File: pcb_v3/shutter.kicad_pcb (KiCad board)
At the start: 2 copper layers, 39 parts, among them IC1 ATMEGA328P-A, K1 FINDER-36.11, K2 FINDER-36.11, K3 HF49FD, P1 5V_IN, P2 GND5, P3 TX/RX, P4 CONN_01X05, P5 ISP, P6 ANT, P7 NETZ_N, P8 NETZ_L, P9 MOTOR, Q1 BC817, Q2 BC817, Q3 BC817, Y1 8MHZ

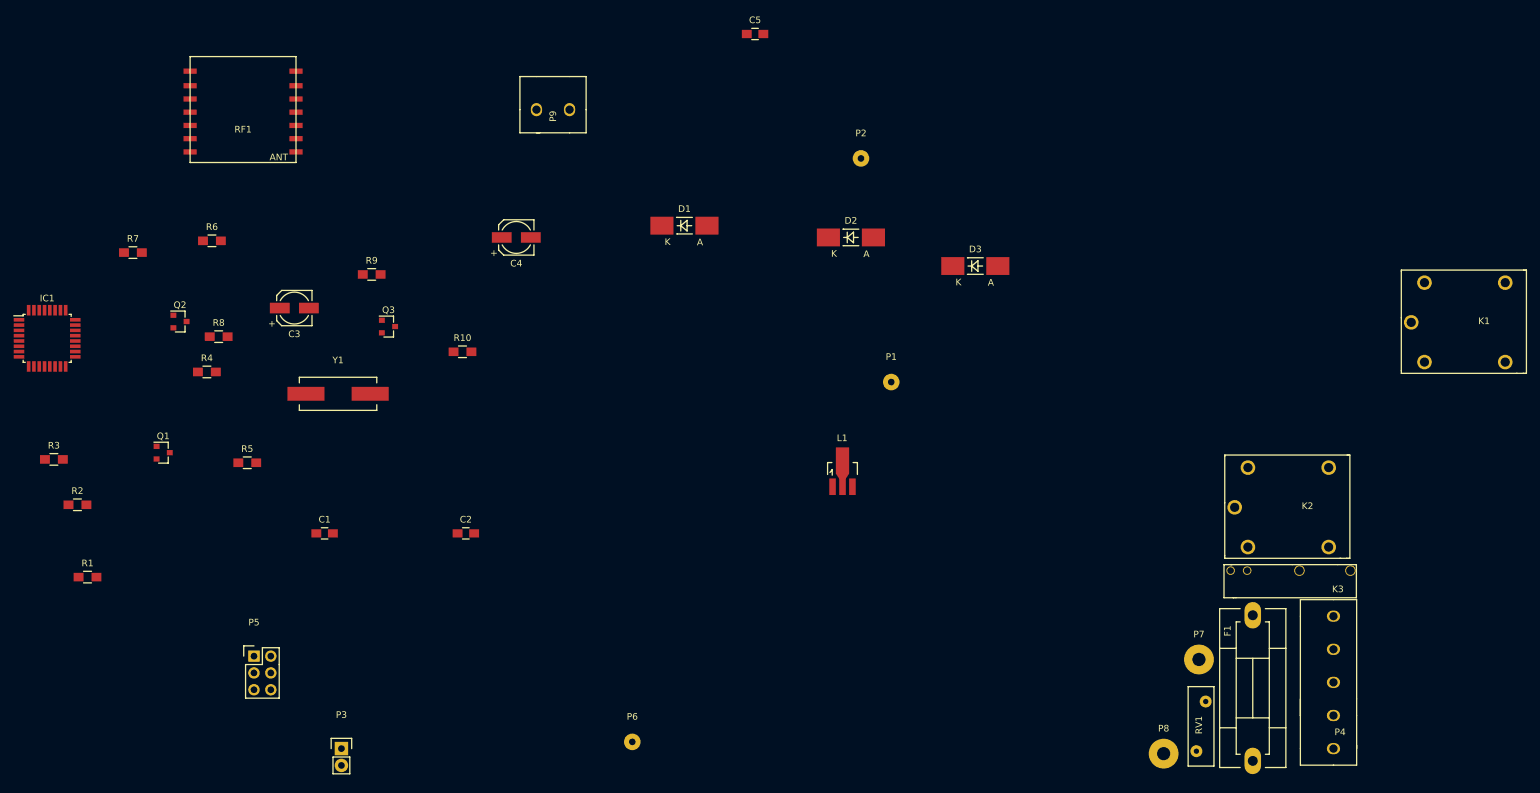
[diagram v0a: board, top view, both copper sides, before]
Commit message: added new Pcb
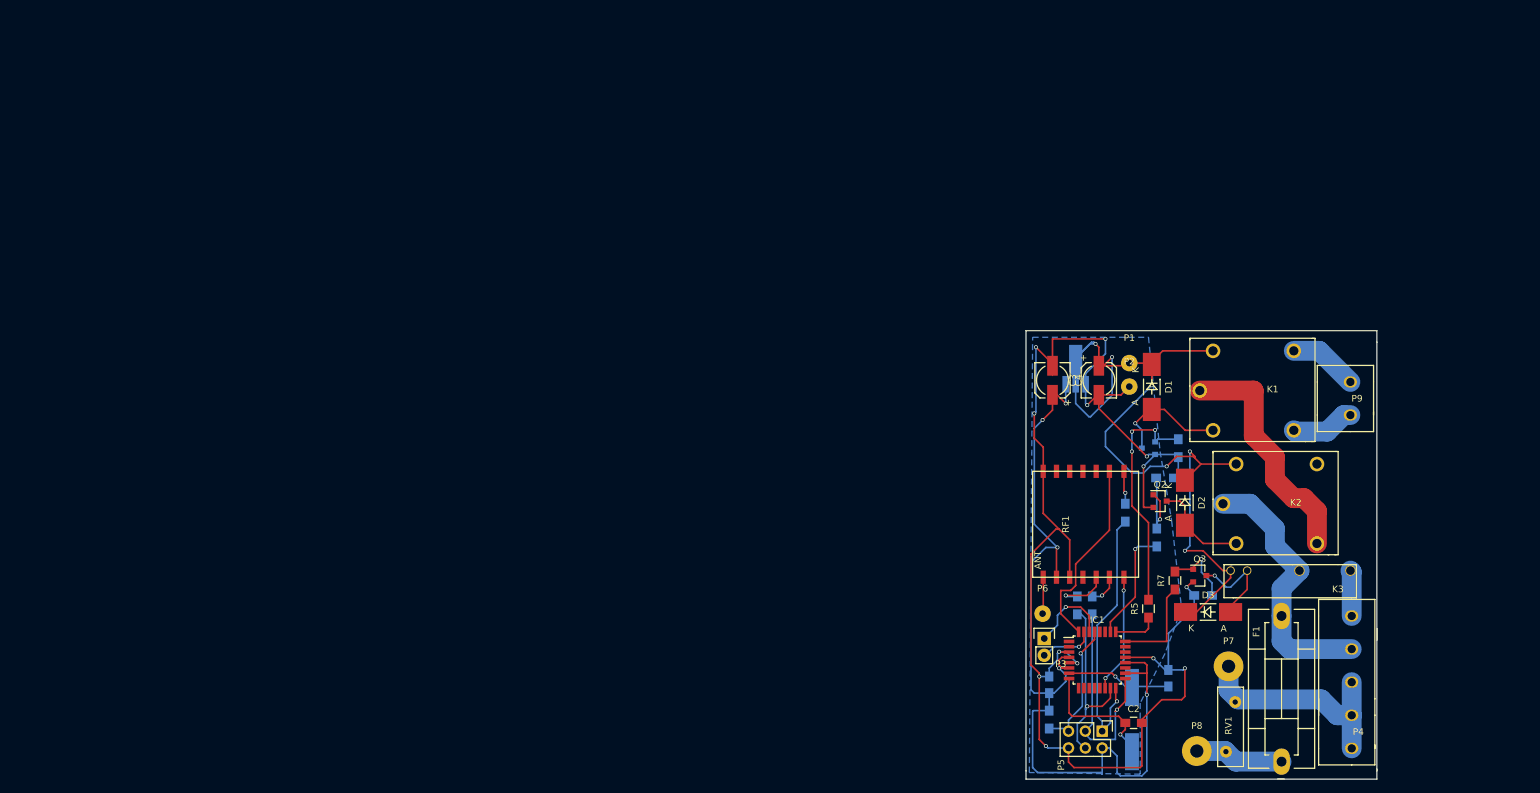
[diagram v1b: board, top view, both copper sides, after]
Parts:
- C1, C5, L1, Q1, R1, R10, R2, R3, R4, R6, R8, R9, Y1: moved to B.Cu
- moved IC1 165.9 mm to (214.8, 122.2)
- moved R7 165.0 mm to (226.5, 110.2), turned to 90 degrees
- moved R3 158.4 mm to (214.0, 114.0), turned to 270 degrees
- moved R2 158.3 mm to (219.0, 100.0), turned to 270 degrees
- moved Q2 150.5 mm to (224.2, 98.2)
- moved R6 149.6 mm to (223.8, 103.8), turned to 90 degrees
- moved Q1 148.8 mm to (222.5, 90.2), turned to 180 degrees
- moved RF1 147.2 mm to (214.0, 93.8), turned to 270 degrees
- moved R1 146.9 mm to (207.5, 131.2), turned to 270 degrees
- moved R8 144.5 mm to (225.0, 94.8), turned to 180 degrees
- moved R5 137.9 mm to (222.5, 114.5), turned to 90 degrees
- moved R4 136.1 mm to (211.8, 114.0), turned to 270 degrees
- moved P9 131.3 mm to (253.0, 85.2), turned to 90 degrees
- moved Y1 129.6 mm to (220.0, 131.2), turned to 270 degrees
- moved C1 129.3 mm to (225.5, 125.0), turned to 90 degrees
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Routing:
- net GND: track 0.00 -> 214.3 mm, vias 0 -> 13
- net 3.3V: track 0.00 -> 135.5 mm, vias 0 -> 5
- net 5V: track 0.00 -> 127.9 mm, vias 0 -> 6
- net MISO: track 0.00 -> 41.2 mm, vias 0 -> 1
- net L: track 0.00 -> 40.2 mm
- net Net-(K1-Pad11): track 0.00 -> 36.1 mm
- net Net-(Q1-Pad1): track 0.00 -> 35.5 mm, vias 0 -> 3
- net SCK: track 0.00 -> 33.9 mm, vias 0 -> 1
- net Net-(P4-Pad1): track 0.00 -> 33.8 mm
- net Net-(IC1-Pad32): track 0.00 -> 29.3 mm
- net MOSI: track 0.00 -> 28.4 mm, vias 0 -> 1
- net RST: track 0.00 -> 19.9 mm, vias 0 -> 1
- net XTAL2: track 0.00 -> 19.7 mm, vias 0 -> 1
- net Net-(D1-Pad2): track 0.00 -> 18.1 mm, vias 0 -> 1
- net NSS: track 0.00 -> 17.9 mm, vias 0 -> 2
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- added copper zone on B.Cu, net GND
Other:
- board outline added: 53 x 67.8 mm
- net class 220 added: clearance 1.5, trace_width 3, via_dia 0.6, via_drill 0.4
- net class std added: clearance 0.2, trace_width 0.25, via_dia 0.6, via_drill 0.4

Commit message: updated pcb
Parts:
- moved P9 1.75 mm to (253.0, 83.5)
- moved P4 0.45 mm to (253.0, 136.0)
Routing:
- net Net-(K1-Pad14): track 10.5 -> 9.77 mm
- net Net-(K1-Pad12): track 9.67 -> 10.2 mm
- net L: track 40.2 -> 39.7 mm
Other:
- net class Default: clearance 0.2 -> 1.3; trace_width 0.25 -> 3
- rule trace_clearance: 0.2 -> 1.3

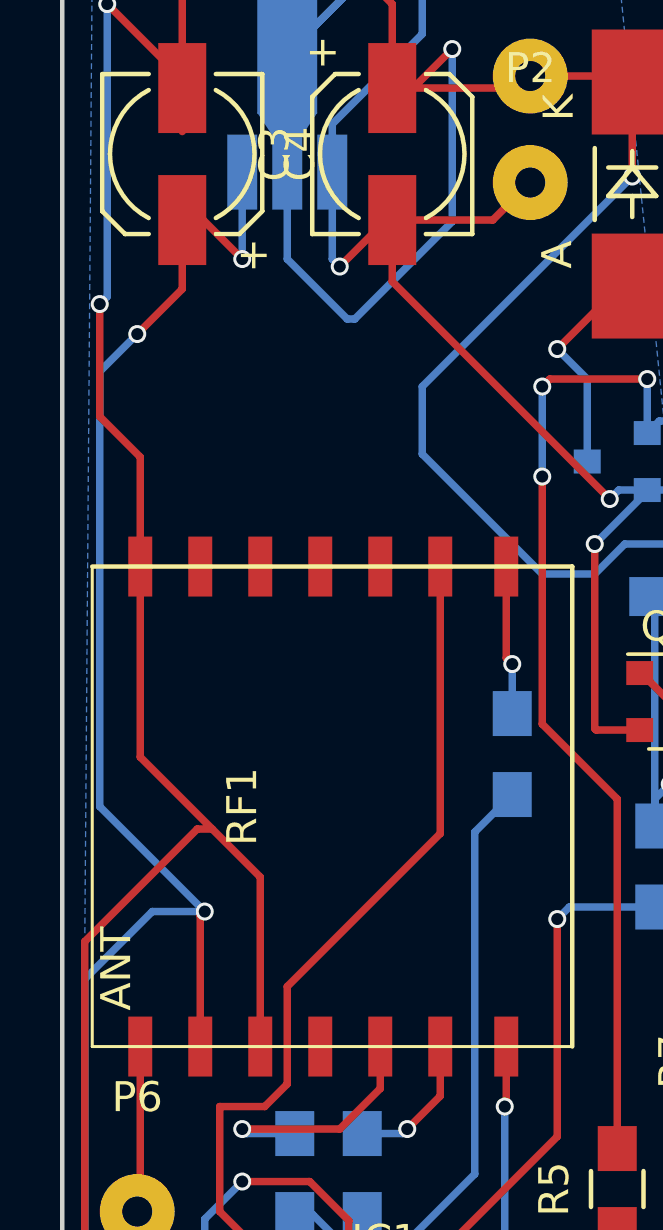
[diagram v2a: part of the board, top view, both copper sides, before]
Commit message: added jumper for power rfm69
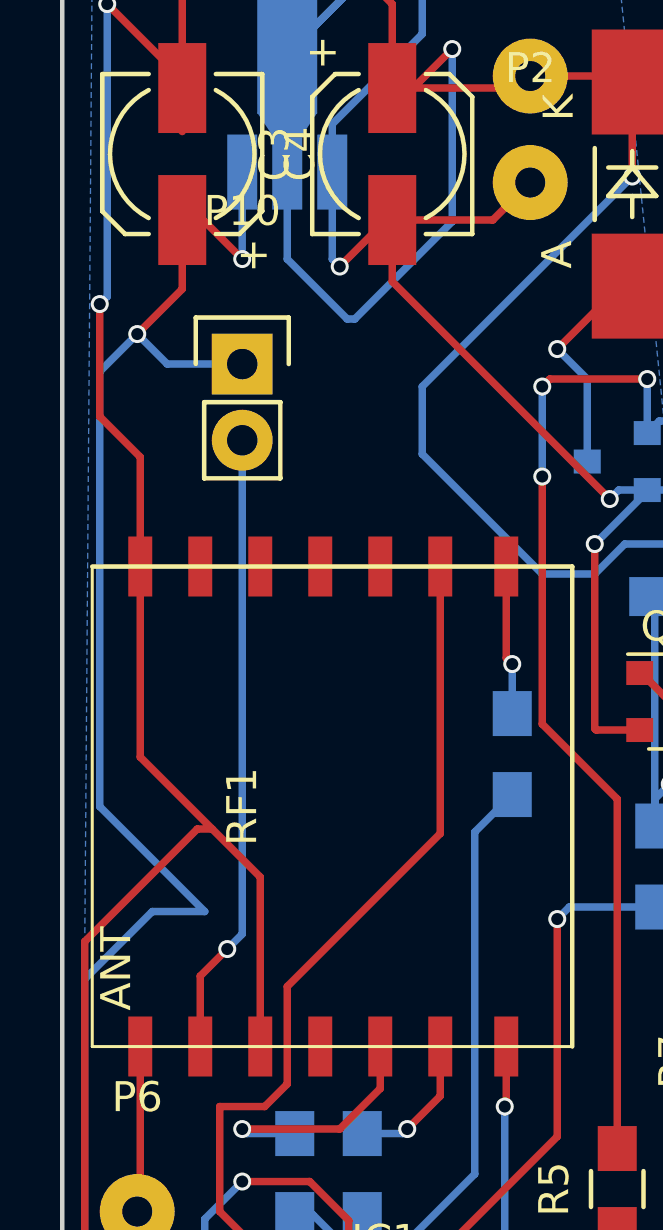
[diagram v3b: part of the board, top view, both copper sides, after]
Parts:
- added P10: ON/OFF, Pin_Headers:Pin_Header_Straight_1x02, F.Cu at (210.0, 87.0)
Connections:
- RF1 pad 2: 3.3V -> Net-(P10-Pad2)
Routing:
- net Net-(P10-Pad2): track 0.00 -> 20.8 mm, vias 0 -> 1
- net 3.3V: track 135.5 -> 134.9 mm, vias 5 -> 4
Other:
- net class Default: clearance 1.3 -> 0.2; trace_width 3 -> 0.25
- rule trace_clearance: 1.3 -> 0.2
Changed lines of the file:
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@@
 (kicad_pcb (version 4) (host pcbnew 4.0.5+dfsg1-4~bpo8+1)
   (general
-    (links 85)
+    (links 86)
     (no_connects 0)
-    (area 202.892857 70.575 265.656 141.625)
+    (area 203.924999 72.424999 257.075001 140.325001)
     (thickness 1.6)
     (drawings 15)
-    (tracks 404)
+    (tracks 408)
     (zones 0)
-    (modules 39)
-    (nets 52)
+    (modules 40)
+    (nets 53)
   )
   (page A4)
@@
   )
   (setup
-    (last_trace_width 3)
-    (trace_clearance 1.3)
+    (last_trace_width 0.25)
+    (trace_clearance 0.2)
     (zone_clearance 0.508)
     (zone_45_only no)
@@
   (net 50 "Net-(RF1-Pad10)")
   (net 51 "Net-(RF1-Pad4)")
+  (net 52 "Net-(P10-Pad2)")
   (net_class Default "This is the default net class."
-    (clearance 1.3)
-    (trace_width 3)
+    (clearance 0.2)
+    (trace_width 0.25)
     (via_dia 0.6)
     (via_drill 0.4)
@@
     (add_net "Net-(K1-Pad14)")
     (add_net "Net-(K2-Pad14)")
+    (add_net "Net-(P10-Pad2)")
     (add_net "Net-(P4-Pad1)")
     (add_net "Net-(P6-Pad1)")
@@
       (net 51 "Net-(RF1-Pad4)"))
     (pad 2 connect rect (at 16 5.4 270) (size 2 0.8) (layers F.Cu F.Mask)
-      (net 5 3.3V))
+      (net 52 "Net-(P10-Pad2)"))
     (pad 1 connect rect (at 16 7.4 270) (size 2 0.8) (layers F.Cu F.Mask)
       (net 40 "Net-(P6-Pad1)"))
@@
     (pad 1 thru_hole oval (at 0 0 90) (size 1.7 2) (drill 1.25) (layers *.Cu *.Mask)
       (net 34 "Net-(K1-Pad12)"))
+  )
+  (module Pin_Headers:Pin_Header_Straight_1x02 (layer F.Cu)
+    (at 210 87)
+    (descr "Through hole pin header")
+    (tags "pin header")
+    (fp_text reference P10 (at 0 -5.1) (layer F.SilkS)
+      (effects (font (size 1 1) (thickness 0.15)))
+    )
+    (fp_text value ON/OFF (at 0 -3.1) (layer F.Fab)
+      (effects (font (size 1 1) (thickness 0.15)))
+    )
+    (fp_line (start 1.27 1.27) (end 1.27 3.81) (layer F.SilkS) (width 0.15))
+    (fp_line (start 1.55 -1.55) (end 1.55 0) (layer F.SilkS) (width 0.15))
+    (fp_line (start -1.75 -1.75) (end -1.75 4.3) (layer F.CrtYd) (width 0.05))
+    (fp_line (start 1.75 -1.75) (end 1.75 4.3) (layer F.CrtYd) (width 0.05))
+    (fp_line (start -1.75 -1.75) (end 1.75 -1.75) (layer F.CrtYd) (width 0.05))
+    (fp_line (start -1.75 4.3) (end 1.75 4.3) (layer F.CrtYd) (width 0.05))
+    (fp_line (start 1.27 1.27) (end -1.27 1.27) (layer F.SilkS) (width 0.15))
+    (fp_line (start -1.55 0) (end -1.55 -1.55) (layer F.SilkS) (width 0.15))
+    (fp_line (start -1.55 -1.55) (end 1.55 -1.55) (layer F.SilkS) (width 0.15))
+    (fp_line (start -1.27 1.27) (end -1.27 3.81) (layer F.SilkS) (width 0.15))
+    (fp_line (start -1.27 3.81) (end 1.27 3.81) (layer F.SilkS) (width 0.15))
+    (pad 1 thru_hole rect (at 0 0) (size 2.032 2.032) (drill 1.016) (layers *.Cu *.Mask)
+      (net 5 3.3V))
+    (pad 2 thru_hole oval (at 0 2.54) (size 2.032 2.032) (drill 1.016) (layers *.Cu *.Mask)
+      (net 52 "Net-(P10-Pad2)"))
+    (model Pin_Headers.3dshapes/Pin_Header_Straight_1x02.wrl
+      (at (xyz 0 -0.05 0))
+      (scale (xyz 1 1 1))
+      (rotate (xyz 0 0 90))
+    )
   )
   (gr_line (start 257 74.25) (end 257 119.25) (angle 90) (layer Edge.Cuts) (width 0.15))
@@
   (segment (start 222.80106 77.4) (end 224.65106 75.55) (width 0.25) (layer F.Cu) (net 4))
   (segment (start 224.65106 75.55) (end 232.25 75.55) (width 0.25) (layer F.Cu) (net 4))
+  (segment (start 210 87) (end 207.5 87) (width 0.25) (layer B.Cu) (net 5) (status 400000))
+  (segment (start 207.5 87) (end 206.5 86) (width 0.25) (layer B.Cu) (net 5))
   (segment (start 209.99886 80.60204) (end 209.99886 83.49886) (width 0.25) (layer B.Cu) (net 5))
   (segment (start 210 83.5) (end 208.7 82.2) (width 0.25) (layer F.Cu) (net 5))
@@
   (segment (start 207 105.25) (end 204.75 107.5) (width 0.25) (layer B.Cu) (net 5))
   (segment (start 208 82.2) (end 208 84.5) (width 0.25) (layer F.Cu) (net 5))
-  (segment (start 208.6 105.4) (end 208.6 109.75) (width 0.25) (layer F.Cu) (net 5))
-  (segment (start 208.75 105.25) (end 208.6 105.4) (width 0.25) (layer F.Cu) (net 5))
-  (via (at 208.75 105.25) (size 0.6) (drill 0.4) (layers F.Cu B.Cu) (net 5))
   (segment (start 205.25 101.75) (end 208.75 105.25) (width 0.25) (layer B.Cu) (net 5))
   (segment (start 205.25 87.25) (end 205.25 101.75) (width 0.25) (layer B.Cu) (net 5))
@@
   (segment (start 234.90106 114.09894) (end 237.406 111.594) (width 0.25) (layer F.Cu) (net 8))
   (segment (start 237.406 111.594) (end 237.406 108.748) (width 0.25) (layer F.Cu) (net 8))
-  (segment (start 242.6 115.59926) (end 242.6 118.6) (width 3) (layer B.Cu) (net 9) (status 400000))
-  (segment (start 245 121) (end 253 121) (width 3) (layer B.Cu) (net 9) (status 800000))
+  (segment (start 242.6 115.59926) (end 242.6 118.6) (width 3) (layer B.Cu) (net 9))
+  (segment (start 245 121) (end 253 121) (width 3) (layer B.Cu) (net 9))
   (segment (start 242.6 118.6) (end 245 121) (width 3) (layer B.Cu) (net 9))
   (segment (start 233.75 98.65) (end 237.85 98.65) (width 3) (layer B.Cu) (net 9))
@@
   (segment (start 216.6 102.65) (end 211.5 107.75) (width 0.25) (layer F.Cu) (net 33))
   (segment (start 211.95 117.95) (end 211.95 118) (width 0.25) (layer F.Cu) (net 33))
-  (segment (start 244.45 87.55) (end 244.95 87.55) (width 3) (layer B.Cu) (net 34) (status C00000))
-  (segment (start 244.95 87.55) (end 247.5 85) (width 3) (layer B.Cu) (net 34) (status 400000))
+  (segment (start 244.45 87.55) (end 244.95 87.55) (width 3) (layer B.Cu) (net 34))
+  (segment (start 244.95 87.55) (end 247.5 85) (width 3) (layer B.Cu) (net 34))
   (segment (start 247.5 85) (end 251.5 85) (width 3) (layer B.Cu) (net 34))
-  (segment (start 251.5 85) (end 253 83.5) (width 3) (layer B.Cu) (net 34) (status 800000))
+  (segment (start 251.5 85) (end 253 83.5) (width 3) (layer B.Cu) (net 34))
   (segment (start 247.95 104.65) (end 247.95 99.75) (width 3) (layer F.Cu) (net 35))
   (segment (start 238.35 81.55) (end 230.25 81.55) (width 3) (layer F.Cu) (net 35))
@@
   (segment (start 246 97.8) (end 244.4 97.8) (width 3) (layer F.Cu) (net 35))
   (segment (start 247.95 99.75) (end 246 97.8) (width 3) (layer F.Cu) (net 35))
-  (segment (start 253 78.5) (end 252.5 78.5) (width 3) (layer B.Cu) (net 36) (status C00000))
-  (segment (start 252.5 78.5) (end 249.55 75.55) (width 3) (layer B.Cu) (net 36) (status 400000))
-  (segment (start 249.55 75.55) (end 244.45 75.55) (width 3) (layer B.Cu) (net 36) (status 800000))
-  (segment (start 253.006 108.748) (end 253.006 115.994) (width 3) (layer B.Cu) (net 38) (status C00000))
-  (segment (start 253.006 115.994) (end 253 116) (width 3) (layer B.Cu) (net 38) (status C00000))
-  (segment (start 235.6 128.6) (end 247.1 128.6) (width 3) (layer B.Cu) (net 39) (status 400000))
-  (segment (start 249 130.5) (end 252.5 130.5) (width 3) (layer B.Cu) (net 39) (status 800000))
+  (segment (start 253 78.5) (end 252.5 78.5) (width 3) (layer B.Cu) (net 36))
+  (segment (start 252.5 78.5) (end 249.55 75.55) (width 3) (layer B.Cu) (net 36))
+  (segment (start 249.55 75.55) (end 244.45 75.55) (width 3) (layer B.Cu) (net 36))
+  (segment (start 253.006 108.748) (end 253.006 115.994) (width 3) (layer B.Cu) (net 38))
+  (segment (start 253.006 115.994) (end 253 116) (width 3) (layer B.Cu) (net 38))
+  (segment (start 235.6 128.6) (end 247.1 128.6) (width 3) (layer B.Cu) (net 39))
+  (segment (start 249 130.5) (end 252.5 130.5) (width 3) (layer B.Cu) (net 39))
   (segment (start 247.1 128.6) (end 249 130.5) (width 3) (layer B.Cu) (net 39))
-  (segment (start 252.5 130.5) (end 253 131) (width 3) (layer B.Cu) (net 39) (status C00000))
-  (segment (start 253 126) (end 253 131) (width 3) (layer B.Cu) (net 39) (status C00000))
-  (segment (start 253 131) (end 253 136) (width 3) (layer B.Cu) (net 39) (status C00000))
+  (segment (start 252.5 130.5) (end 253 131) (width 3) (layer B.Cu) (net 39))
+  (segment (start 253 126) (end 253 131) (width 3) (layer B.Cu) (net 39))
+  (segment (start 253 131) (end 253 136) (width 3) (layer B.Cu) (net 39))
   (segment (start 236 128.2) (end 234.6 126.8) (width 3) (layer B.Cu) (net 39))
   (segment (start 234.6 126.8) (end 234.6 123.2) (width 3) (layer B.Cu) (net 39))
@@
   (segment (start 213.25 112.5) (end 210 112.5) (width 0.25) (layer F.Cu) (net 46))
   (segment (start 214.6 111.15) (end 213.25 112.5) (width 0.25) (layer F.Cu) (net 46))
+  (segment (start 208.6 109.75) (end 208.6 107.4) (width 0.25) (layer F.Cu) (net 52) (status 400000))
+  (segment (start 210 106) (end 210 89.54) (width 0.25) (layer B.Cu) (net 52) (status 800000))
+  (segment (start 209.5 106.5) (end 210 106) (width 0.25) (layer B.Cu) (net 52))
+  (via (at 209.5 106.5) (size 0.6) (drill 0.4) (layers F.Cu B.Cu) (net 52))
+  (segment (start 208.6 107.4) (end 209.5 106.5) (width 0.25) (layer F.Cu) (net 52))
   (zone (net 2) (net_name GND) (layer B.Cu) (hatch edge 0.508)
     (connect_pads (clearance 0.508))
